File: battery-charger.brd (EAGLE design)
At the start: 23.5 x 29.4 mm, 9 parts, among them J2 10118192-0001LF, U1 MCP73831T-2DCI/OT

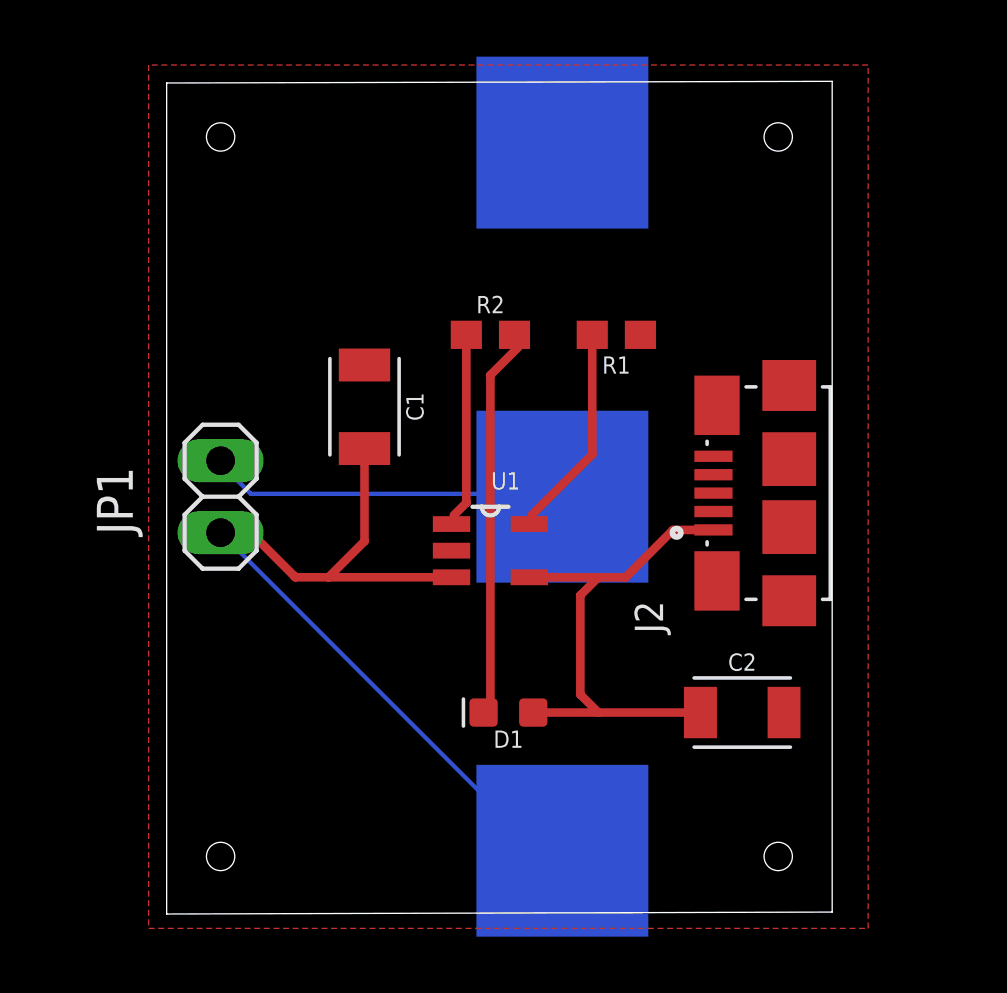
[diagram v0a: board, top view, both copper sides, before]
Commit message: add under charge protection
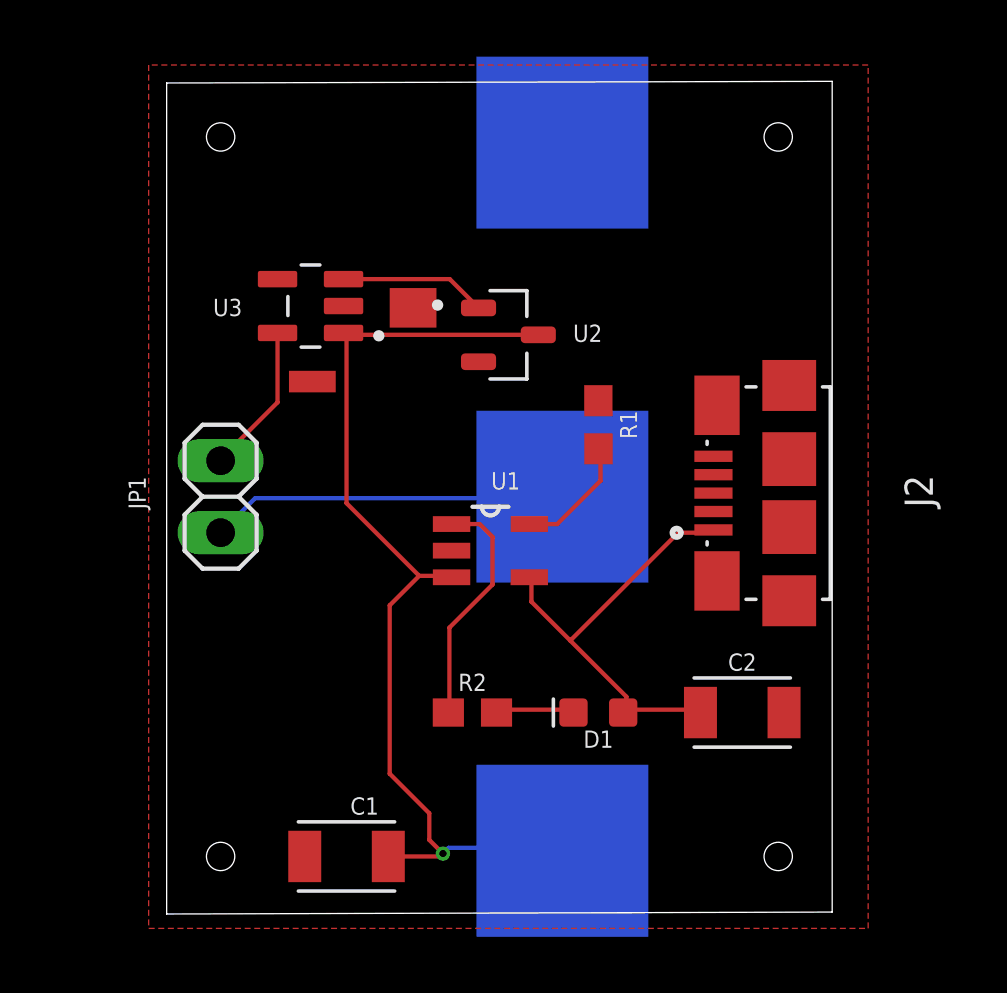
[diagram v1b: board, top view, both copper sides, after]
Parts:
- added U2: MCP112T-270E/TT, MCP112T-270E_TT:SOT95P237X112-3N
- added U3: MIC2004-1.2YM5-TR, MIC2004-1.2YM5-TR:SOT95P280X145-5N
- moved C1 15.9 mm to (27.3, 15.2), turned to 0 degrees
- moved R2 13.4 mm to (31.8, 20.3)
- moved R1 3.24 mm to (36.2, 30.5), turned to 270 degrees
- moved D1 3.17 mm to (36.2, 20.3)
- turned JP1 to 270 degrees
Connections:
- new net ENABLE: U2.1, U3.3
- new net VOUT: JP1.1, U3.5
- net GND: now also U2.2, U3.2
- net VBAT: now also U2.3, U3.1; no longer JP1.1
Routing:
- net N$3: track 13.9 -> 2.85 mm
- net VOUT: track 0.00 -> 5.34 mm
- net ENABLE: track 0.00 -> 5.19 mm
- net N$1: track 7.65 -> 4.31 mm
- net +5V: track 18.4 -> 15.6 mm
- net N$4: track 6.95 -> 8.47 mm
- net VBAT: track 36.2 -> 35.1 mm, vias 0 -> 1

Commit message: add on / off switch to charger
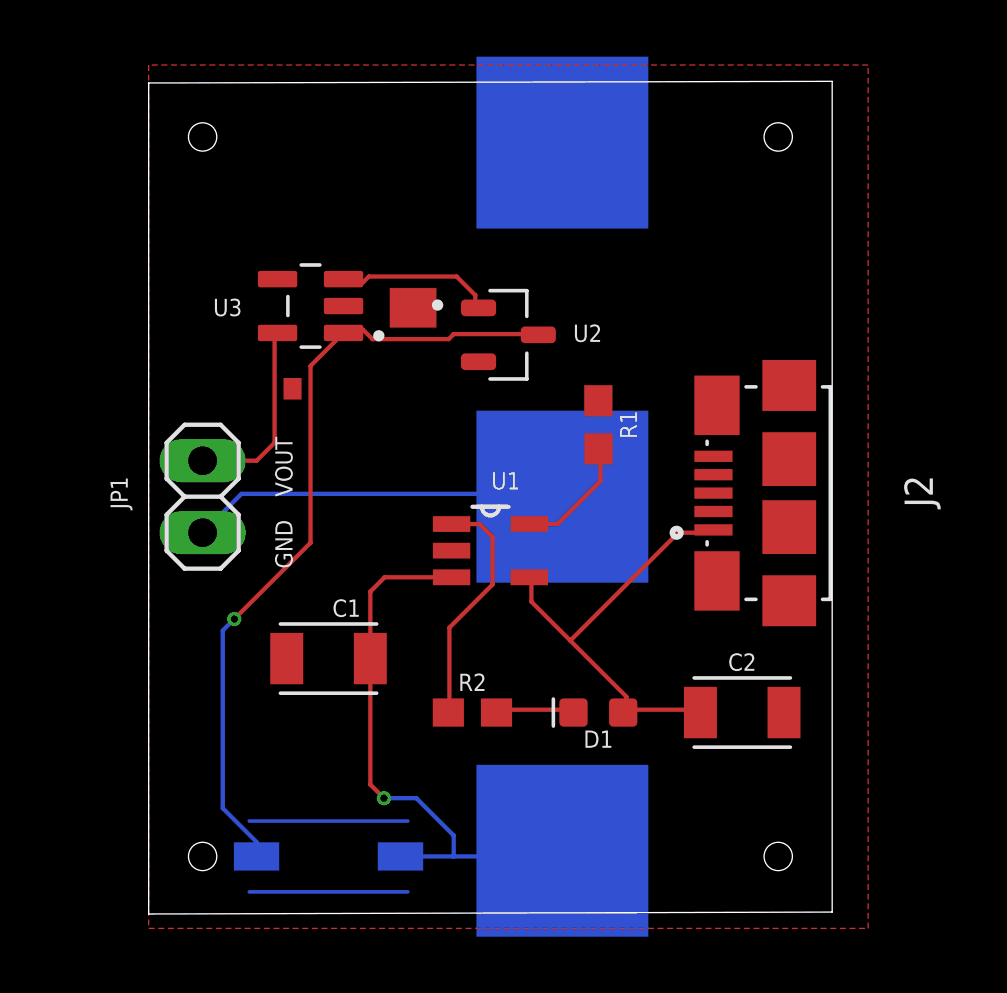
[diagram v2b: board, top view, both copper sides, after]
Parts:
- added U$1: CHS-01TASMD, CHS-01TA:CHS-01TA
- moved C1 7.01 mm to (26.7, 22.2)
- moved JP1 0.63 mm to (22.2, 27.9)
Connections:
- new net VBAT_SWITCH: U$1.S0, U2.3, U3.1
- net VBAT: now also U$1.SI; no longer U2.3, U3.1
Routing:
- net VBAT_SWITCH: track 0.00 -> 27.9 mm, vias 0 -> 1
- net VBAT: track 35.1 -> 20.1 mm
- net VOUT: track 5.34 -> 6.71 mm
- net GND: track 12.6 -> 13.3 mm
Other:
- board size 23.5 x 29.4 mm -> 24.1 x 29.4 mm
- board text added: "GND"
- board text added: "VOUT"

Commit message: finalize battery charger
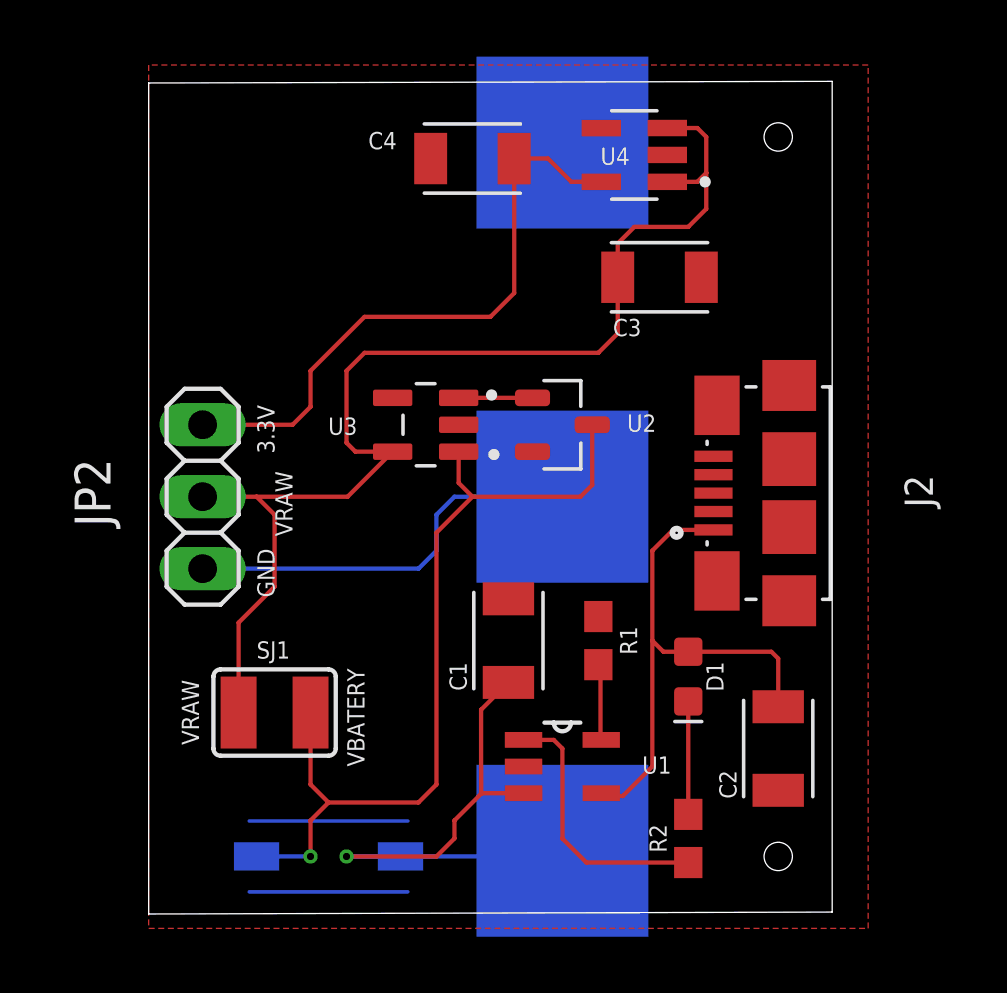
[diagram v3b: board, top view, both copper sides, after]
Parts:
- removed JP1: (no value), pinhead:1X02
- added C3, C4: 1uF, Capacitor:CAPC3216X135
- added JP2: (no value), pinhead:1X03
- added SJ1: (no value), jumper:SJW
- added U4: MIC5504-3.3YM5-T5, MIC5504-3.3YM5-T5:SOT95P280X145-5N
- moved R2 8.82 mm to (39.4, 15.9), turned to 90 degrees
- moved U1 8.03 mm to (34.9, 18.4)
- moved R1 7.62 mm to (36.2, 22.9)
- moved C1 6.38 mm to (33.0, 22.9), turned to 270 degrees
- moved U3 5.84 mm to (30.1, 30.5)
- moved U2 3.70 mm to (34.9, 30.5)
- moved D1 3.42 mm to (39.4, 21.6), turned to 270 degrees
- moved C2 1.80 mm to (42.5, 19.1), turned to 270 degrees
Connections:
- removed net VOUT: JP1.1, U3.5
- new net +3V3: C4.1, JP2.1, U4.5
- new net VRAW: C3.1, JP2.2, SJ1.1, U3.5, U4.1, U4.3
- net GND: now also C3.2, C4.2, JP2.3, U4.2; no longer JP1.2
- net VBAT_SWITCH: now also SJ1.2
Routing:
- net VRAW: track 0.00 -> 42.6 mm
- net +3V3: track 0.00 -> 21.8 mm
- net VOUT: track 6.71 -> 0.00 mm
- net +5V: track 15.6 -> 18.8 mm
- net ENABLE: track 5.55 -> 2.61 mm
- net VBAT_SWITCH: track 27.9 -> 30.6 mm
- net N$1: track 4.31 -> 2.70 mm
- net GND: track 13.3 -> 14.5 mm
- net N$3: track 2.85 -> 3.99 mm
- net N$4: track 8.47 -> 9.47 mm
- net VBAT: track 20.1 -> 19.6 mm
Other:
- board text added: "3.3V"
- board text added: "VBATERY"
- board text added: "VRAW"
- board text removed: "VOUT"
